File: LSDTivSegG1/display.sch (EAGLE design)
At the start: 123 parts, among them IC1 MEGA8-P, IC2 MAX232, IC3 PCF8574P, IC4 PCF8574P, IC5 PCF8574P, IC6 PCF8574P, T1 BC847, T10 BC847, T11 BC847, T12 BC847, T13 BC847, T14 BC847, T15 BC847, T16 BC847, T17 BC847, T18 BC847, T19 BC847, T2 BC847, T20 BC847, T21 BC847, T22 BC847, T23 BC847, T24 BC847, T3 BC847, T4 BC847, T5 BC847, T6 BC847, T7 BC847, T8 BC847, T9 BC847

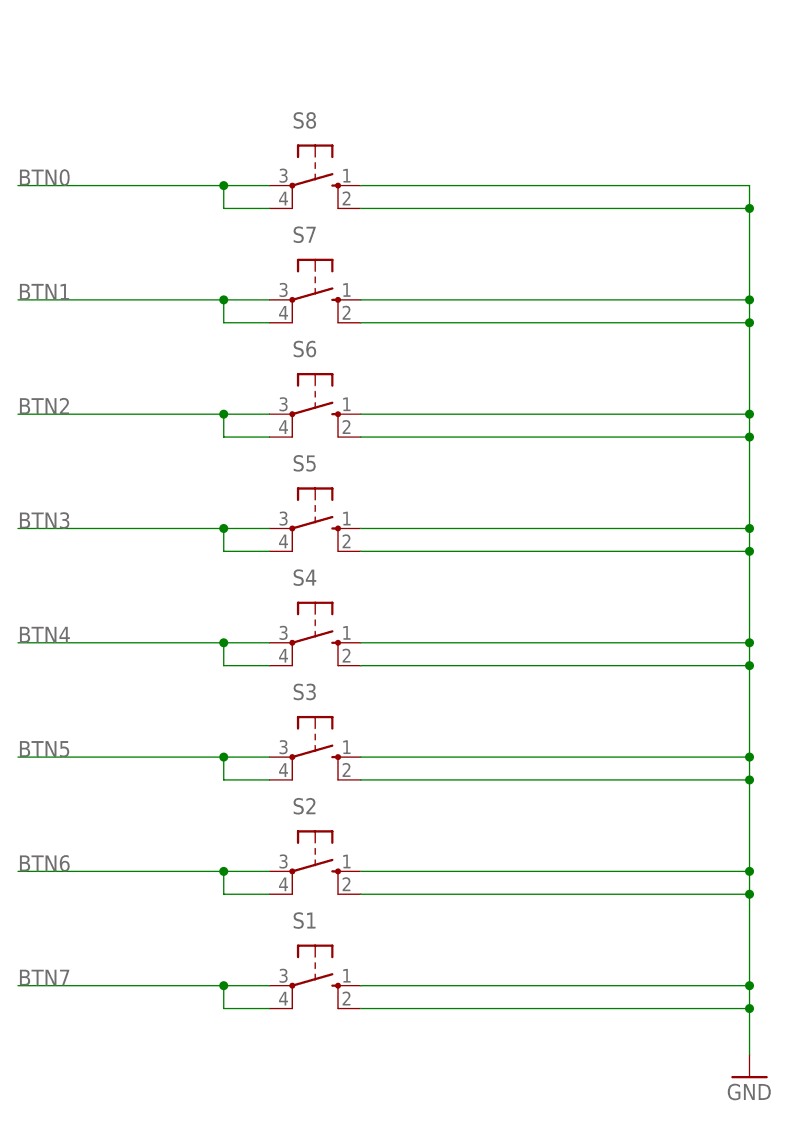
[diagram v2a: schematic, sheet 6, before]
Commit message: finished routing there just some wire stubs to remove (DRC)
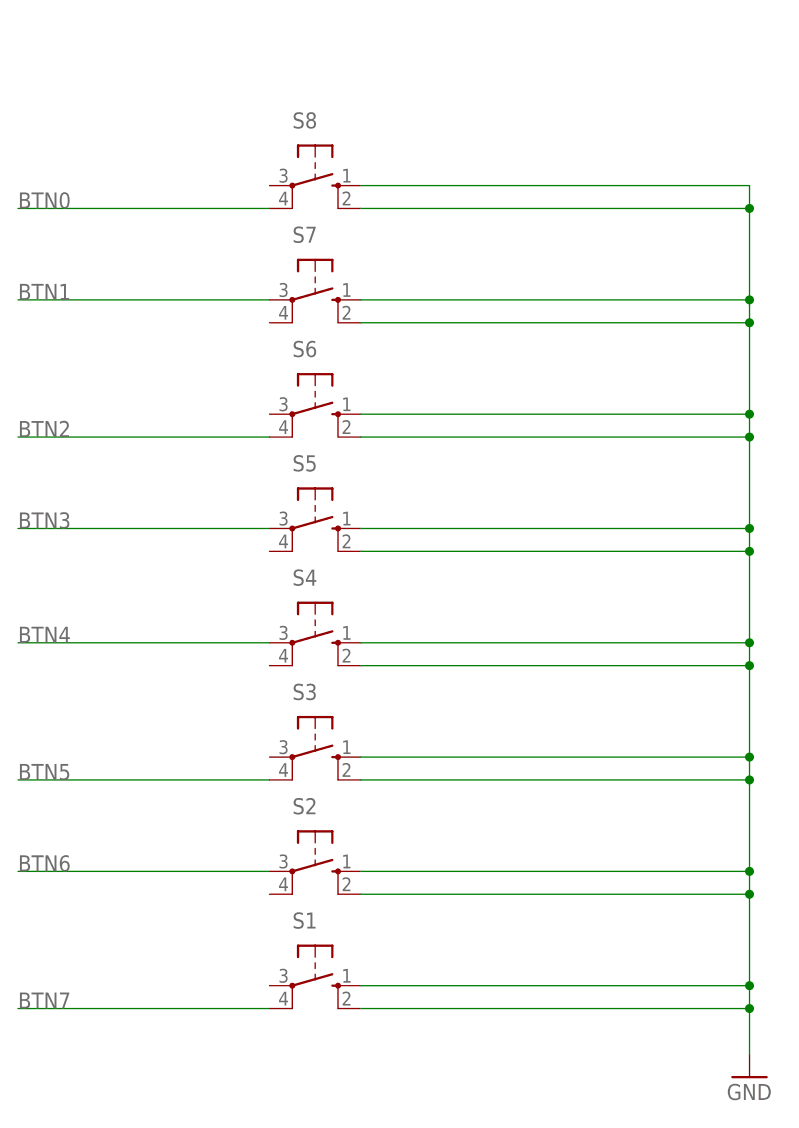
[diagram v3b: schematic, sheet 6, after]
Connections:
- net BTN0: no longer S8.P
- net BTN1: no longer S7.P1
- net BTN2: no longer S6.P
- net BTN3: no longer S5.P1
- net BTN4: no longer S4.P1
- net BTN5: no longer S3.P
- net BTN6: no longer S2.P1
- net BTN7: no longer S1.P
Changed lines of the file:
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@@
 <net name="BTN0" class="0">
 <segment>
-<pinref part="S8" gate="1" pin="P"/>
-<wire x1="63.5" y1="33.02" x2="58.42" y2="33.02" width="0.1524" layer="91"/>
 <pinref part="S8" gate="1" pin="P1"/>
-<wire x1="58.42" y1="33.02" x2="35.56" y2="33.02" width="0.1524" layer="91"/>
-<wire x1="63.5" y1="30.48" x2="58.42" y2="30.48" width="0.1524" layer="91"/>
-<wire x1="58.42" y1="30.48" x2="58.42" y2="33.02" width="0.1524" layer="91"/>
-<junction x="58.42" y="33.02"/>
-<label x="35.56" y="33.02" size="1.778" layer="95"/>
+<wire x1="63.5" y1="30.48" x2="35.56" y2="30.48" width="0.1524" layer="91"/>
+<label x="35.56" y="30.48" size="1.778" layer="95"/>
 </segment>
 </net>
@@
 <segment>
 <pinref part="S7" gate="1" pin="P"/>
-<wire x1="63.5" y1="20.32" x2="58.42" y2="20.32" width="0.1524" layer="91"/>
-<pinref part="S7" gate="1" pin="P1"/>
-<wire x1="58.42" y1="20.32" x2="35.56" y2="20.32" width="0.1524" layer="91"/>
-<wire x1="63.5" y1="17.78" x2="58.42" y2="17.78" width="0.1524" layer="91"/>
-<wire x1="58.42" y1="17.78" x2="58.42" y2="20.32" width="0.1524" layer="91"/>
-<junction x="58.42" y="20.32"/>
+<wire x1="63.5" y1="20.32" x2="35.56" y2="20.32" width="0.1524" layer="91"/>
 <label x="35.56" y="20.32" size="1.778" layer="95"/>
 </segment>
@@
 <net name="BTN2" class="0">
 <segment>
-<pinref part="S6" gate="1" pin="P"/>
-<wire x1="63.5" y1="7.62" x2="58.42" y2="7.62" width="0.1524" layer="91"/>
 <pinref part="S6" gate="1" pin="P1"/>
-<wire x1="58.42" y1="7.62" x2="35.56" y2="7.62" width="0.1524" layer="91"/>
-<wire x1="63.5" y1="5.08" x2="58.42" y2="5.08" width="0.1524" layer="91"/>
-<wire x1="58.42" y1="5.08" x2="58.42" y2="7.62" width="0.1524" layer="91"/>
-<junction x="58.42" y="7.62"/>
-<label x="35.56" y="7.62" size="1.778" layer="95"/>
+<wire x1="63.5" y1="5.08" x2="35.56" y2="5.08" width="0.1524" layer="91"/>
+<label x="35.56" y="5.08" size="1.778" layer="95"/>
 </segment>
 </net>
@@
 <segment>
 <pinref part="S5" gate="1" pin="P"/>
-<wire x1="63.5" y1="-5.08" x2="58.42" y2="-5.08" width="0.1524" layer="91"/>
-<pinref part="S5" gate="1" pin="P1"/>
-<wire x1="58.42" y1="-5.08" x2="35.56" y2="-5.08" width="0.1524" layer="91"/>
-<wire x1="63.5" y1="-7.62" x2="58.42" y2="-7.62" width="0.1524" layer="91"/>
-<wire x1="58.42" y1="-7.62" x2="58.42" y2="-5.08" width="0.1524" layer="91"/>
-<junction x="58.42" y="-5.08"/>
+<wire x1="63.5" y1="-5.08" x2="35.56" y2="-5.08" width="0.1524" layer="91"/>
 <label x="35.56" y="-5.08" size="1.778" layer="95"/>
 </segment>
@@
 <segment>
 <pinref part="S4" gate="1" pin="P"/>
-<wire x1="63.5" y1="-17.78" x2="58.42" y2="-17.78" width="0.1524" layer="91"/>
-<pinref part="S4" gate="1" pin="P1"/>
-<wire x1="58.42" y1="-17.78" x2="35.56" y2="-17.78" width="0.1524" layer="91"/>
-<wire x1="63.5" y1="-20.32" x2="58.42" y2="-20.32" width="0.1524" layer="91"/>
-<wire x1="58.42" y1="-20.32" x2="58.42" y2="-17.78" width="0.1524" layer="91"/>
-<junction x="58.42" y="-17.78"/>
+<wire x1="63.5" y1="-17.78" x2="35.56" y2="-17.78" width="0.1524" layer="91"/>
 <label x="35.56" y="-17.78" size="1.778" layer="95"/>
 </segment>
@@
 <net name="BTN5" class="0">
 <segment>
-<pinref part="S3" gate="1" pin="P"/>
-<wire x1="63.5" y1="-30.48" x2="58.42" y2="-30.48" width="0.1524" layer="91"/>
 <pinref part="S3" gate="1" pin="P1"/>
-<wire x1="58.42" y1="-30.48" x2="35.56" y2="-30.48" width="0.1524" layer="91"/>
-<wire x1="63.5" y1="-33.02" x2="58.42" y2="-33.02" width="0.1524" layer="91"/>
-<wire x1="58.42" y1="-33.02" x2="58.42" y2="-30.48" width="0.1524" layer="91"/>
-<junction x="58.42" y="-30.48"/>
-<label x="35.56" y="-30.48" size="1.778" layer="95"/>
+<wire x1="63.5" y1="-33.02" x2="35.56" y2="-33.02" width="0.1524" layer="91"/>
+<label x="35.56" y="-33.02" size="1.778" layer="95"/>
 </segment>
 </net>
@@
 <segment>
 <pinref part="S2" gate="1" pin="P"/>
-<wire x1="63.5" y1="-43.18" x2="58.42" y2="-43.18" width="0.1524" layer="91"/>
-<pinref part="S2" gate="1" pin="P1"/>
-<wire x1="58.42" y1="-43.18" x2="35.56" y2="-43.18" width="0.1524" layer="91"/>
-<wire x1="63.5" y1="-45.72" x2="58.42" y2="-45.72" width="0.1524" layer="91"/>
-<wire x1="58.42" y1="-45.72" x2="58.42" y2="-43.18" width="0.1524" layer="91"/>
-<junction x="58.42" y="-43.18"/>
+<wire x1="63.5" y1="-43.18" x2="35.56" y2="-43.18" width="0.1524" layer="91"/>
 <label x="35.56" y="-43.18" size="1.778" layer="95"/>
 </segment>
@@
 <net name="BTN7" class="0">
 <segment>
-<pinref part="S1" gate="1" pin="P"/>
-<wire x1="63.5" y1="-55.88" x2="58.42" y2="-55.88" width="0.1524" layer="91"/>
 <pinref part="S1" gate="1" pin="P1"/>
-<wire x1="58.42" y1="-55.88" x2="35.56" y2="-55.88" width="0.1524" layer="91"/>
-<wire x1="63.5" y1="-58.42" x2="58.42" y2="-58.42" width="0.1524" layer="91"/>
-<wire x1="58.42" y1="-58.42" x2="58.42" y2="-55.88" width="0.1524" layer="91"/>
-<junction x="58.42" y="-55.88"/>
-<label x="35.56" y="-55.88" size="1.778" layer="95"/>
+<wire x1="63.5" y1="-58.42" x2="35.56" y2="-58.42" width="0.1524" layer="91"/>
+<label x="35.56" y="-58.42" size="1.778" layer="95"/>
 </segment>
 </net>

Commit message: added pullup resistors to buttons
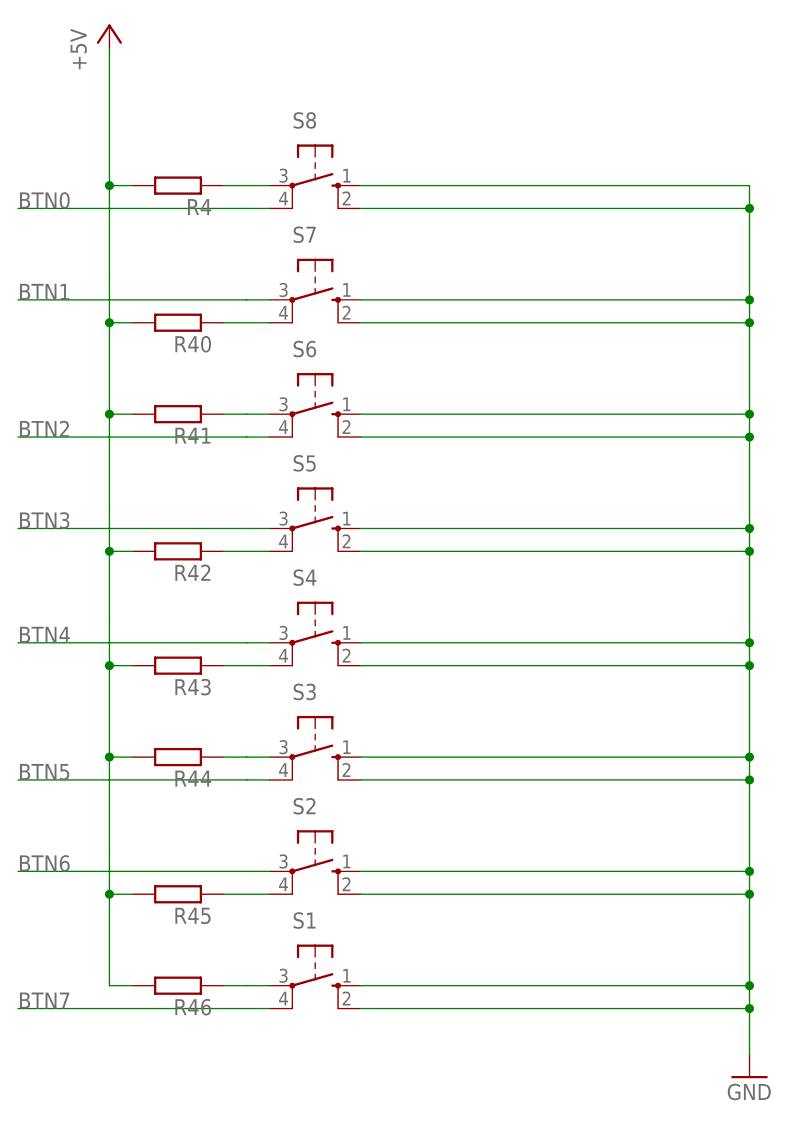
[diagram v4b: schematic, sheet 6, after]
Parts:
- added R4, R40, R41, R42, R43, R44, R45, R46: (no value), rcl:R-EU_R0805
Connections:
- new net N$49: R4.1, S8.P
- new net N$50: R41.1, S6.P
- new net N$52: R45.1, S2.P1
- new net N$76: R43.1, S4.P1
- new net N$77: R44.1, S3.P
- new net N$78: R42.1, S5.P1
- new net N$79: R46.1, S1.P
- new net N$80: R40.1, S7.P1
- net +5V: now also R4.2, R40.2, R41.2, R42.2, R43.2, R44.2, R45.2, R46.2

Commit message: added values to the pullups (buttons)
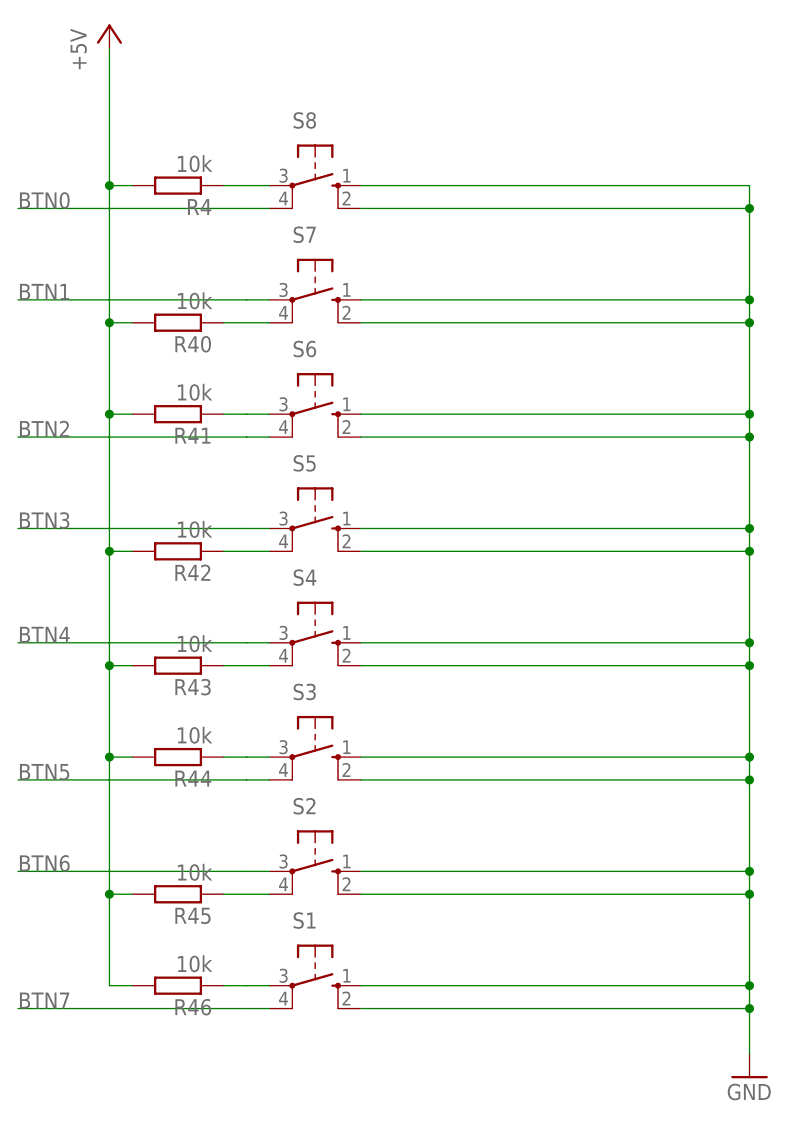
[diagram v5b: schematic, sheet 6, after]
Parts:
- R4, R40, R41, R42, R43, R44, R45, R46: value (none) -> 10k
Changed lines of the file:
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@@
 <part name="P+16" library="supply1" library_urn="urn:adsk.eagle:library:371" deviceset="+5V" device=""/>
 <part name="P+17" library="supply1" library_urn="urn:adsk.eagle:library:371" deviceset="+5V" device=""/>
-<part name="R4" library="rcl" library_urn="urn:adsk.eagle:library:334" deviceset="R-EU_" device="R0805" package3d_urn="urn:adsk.eagle:package:23553/2"/>
-<part name="R40" library="rcl" library_urn="urn:adsk.eagle:library:334" deviceset="R-EU_" device="R0805" package3d_urn="urn:adsk.eagle:package:23553/2"/>
-<part name="R41" library="rcl" library_urn="urn:adsk.eagle:library:334" deviceset="R-EU_" device="R0805" package3d_urn="urn:adsk.eagle:package:23553/2"/>
-<part name="R42" library="rcl" library_urn="urn:adsk.eagle:library:334" deviceset="R-EU_" device="R0805" package3d_urn="urn:adsk.eagle:package:23553/2"/>
-<part name="R43" library="rcl" library_urn="urn:adsk.eagle:library:334" deviceset="R-EU_" device="R0805" package3d_urn="urn:adsk.eagle:package:23553/2"/>
-<part name="R44" library="rcl" library_urn="urn:adsk.eagle:library:334" deviceset="R-EU_" device="R0805" package3d_urn="urn:adsk.eagle:package:23553/2"/>
-<part name="R45" library="rcl" library_urn="urn:adsk.eagle:library:334" deviceset="R-EU_" device="R0805" package3d_urn="urn:adsk.eagle:package:23553/2"/>
-<part name="R46" library="rcl" library_urn="urn:adsk.eagle:library:334" deviceset="R-EU_" device="R0805" package3d_urn="urn:adsk.eagle:package:23553/2"/>
+<part name="R4" library="rcl" library_urn="urn:adsk.eagle:library:334" deviceset="R-EU_" device="R0805" package3d_urn="urn:adsk.eagle:package:23553/2" value="10k"/>
+<part name="R40" library="rcl" library_urn="urn:adsk.eagle:library:334" deviceset="R-EU_" device="R0805" package3d_urn="urn:adsk.eagle:package:23553/2" value="10k"/>
+<part name="R41" library="rcl" library_urn="urn:adsk.eagle:library:334" deviceset="R-EU_" device="R0805" package3d_urn="urn:adsk.eagle:package:23553/2" value="10k"/>
+<part name="R42" library="rcl" library_urn="urn:adsk.eagle:library:334" deviceset="R-EU_" device="R0805" package3d_urn="urn:adsk.eagle:package:23553/2" value="10k"/>
+<part name="R43" library="rcl" library_urn="urn:adsk.eagle:library:334" deviceset="R-EU_" device="R0805" package3d_urn="urn:adsk.eagle:package:23553/2" value="10k"/>
+<part name="R44" library="rcl" library_urn="urn:adsk.eagle:library:334" deviceset="R-EU_" device="R0805" package3d_urn="urn:adsk.eagle:package:23553/2" value="10k"/>
+<part name="R45" library="rcl" library_urn="urn:adsk.eagle:library:334" deviceset="R-EU_" device="R0805" package3d_urn="urn:adsk.eagle:package:23553/2" value="10k"/>
+<part name="R46" library="rcl" library_urn="urn:adsk.eagle:library:334" deviceset="R-EU_" device="R0805" package3d_urn="urn:adsk.eagle:package:23553/2" value="10k"/>
 <part name="P+18" library="supply1" library_urn="urn:adsk.eagle:library:371" deviceset="+5V" device=""/>
 </parts>
